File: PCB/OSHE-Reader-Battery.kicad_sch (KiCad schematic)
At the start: 12 parts, among them Q1 PNP, U1 BQ2057CSNTR, U2 IRF7326D2TRPBF

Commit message: Update OSHE-Reader-Battery.kicad_sch
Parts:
- R3: value R_{T2}/100K -> R_{T2}/10K
- R4: value R_{T1}/100K -> R_{T1}/10K
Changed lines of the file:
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@@
 			)
 		)
-		(property "Value" "R_{T1}/100K"
+		(property "Value" "R_{T1}/10K"
 			(at 41.91 107.9499 0)
 			(effects
@@
 			)
 		)
-		(property "Value" "R_{T2}/100K"
+		(property "Value" "R_{T2}/10K"
 			(at 41.91 92.7099 0)
 			(effects

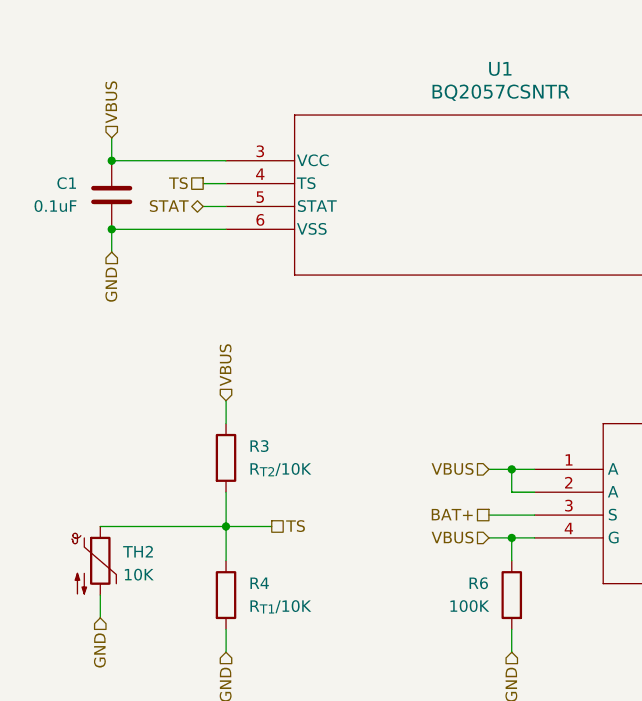
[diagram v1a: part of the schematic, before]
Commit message: removed old battery and thermistor references
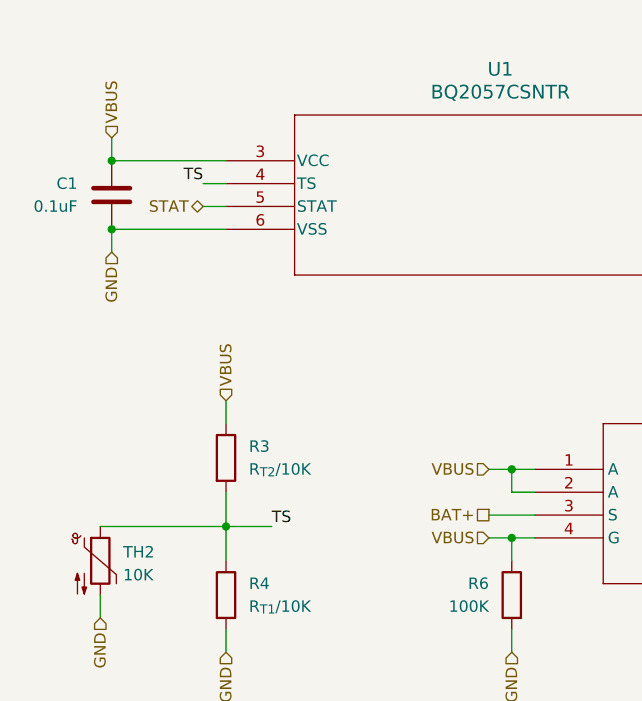
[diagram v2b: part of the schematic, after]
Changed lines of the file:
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@@
+		)
+	)
+	(label "TS"
+		(at 44.45 99.06 0)
+		(effects
+			(font
+				(size 1.27 1.27)
+			)
+			(justify left bottom)
+		)
+	)
+	(label "TS"
+		(at 36.83 60.96 180)
+		(effects
+			(font
+				(size 1.27 1.27)
+			)
+			(justify right bottom)
 		)
 	)
@@
 		)
 	)
-	(hierarchical_label "TS"
-		(shape passive)
-		(at 44.45 99.06 0)
-		(effects
-			(font
-				(size 1.27 1.27)
-			)
-			(justify left)
-		)
-	)
 	(hierarchical_label "VBUS"
 		(shape input)
@@
 		)
 	)
-	(hierarchical_label "TS"
-		(shape passive)
-		(at 36.83 60.96 180)
-		(effects
-			(font
-				(size 1.27 1.27)
-			)
-			(justify right)
-		)
-	)

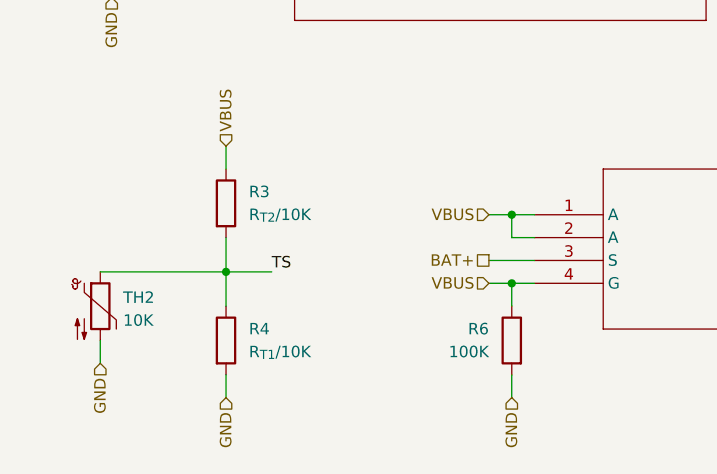
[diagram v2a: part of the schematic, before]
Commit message: Update OSHE-Reader-Battery.kicad_sch
changing resistor value for the thermstor
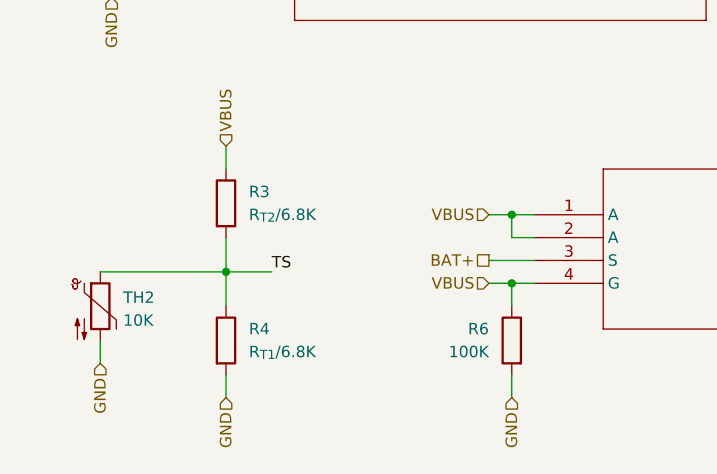
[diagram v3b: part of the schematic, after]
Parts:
- R3: value R_{T2}/10K -> R_{T2}/6.8K
- R4: value R_{T1}/10K -> R_{T1}/6.8K
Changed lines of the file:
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@@
 			)
 		)
-		(property "Value" "R_{T1}/10K"
+		(property "Value" "R_{T1}/6.8K"
 			(at 41.91 107.9499 0)
 			(effects
@@
 			)
 		)
-		(property "Value" "R_{T2}/10K"
+		(property "Value" "R_{T2}/6.8K"
 			(at 41.91 92.7099 0)
 			(effects

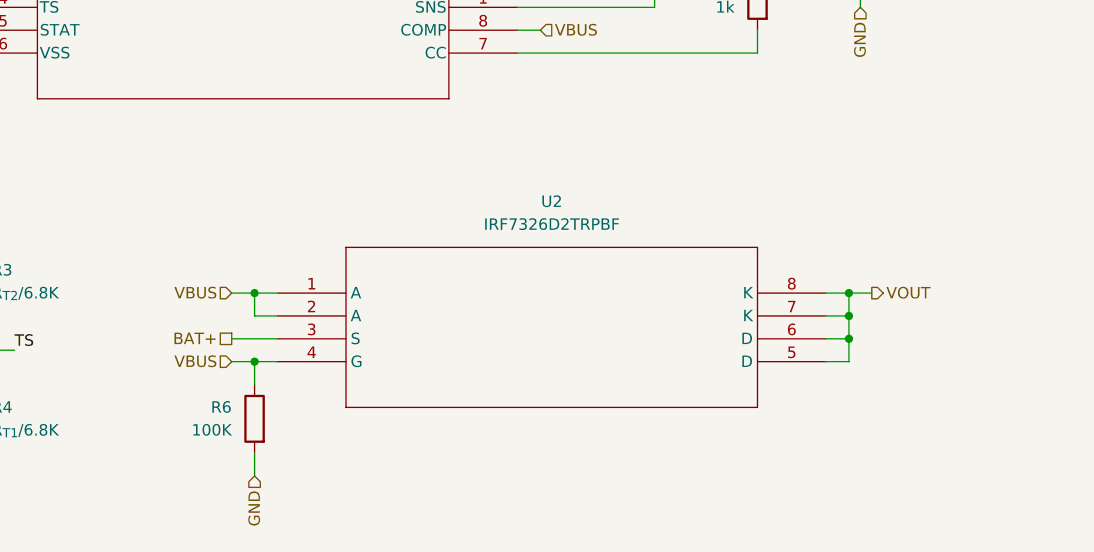
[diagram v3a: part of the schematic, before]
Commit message: Added LED to battery charger
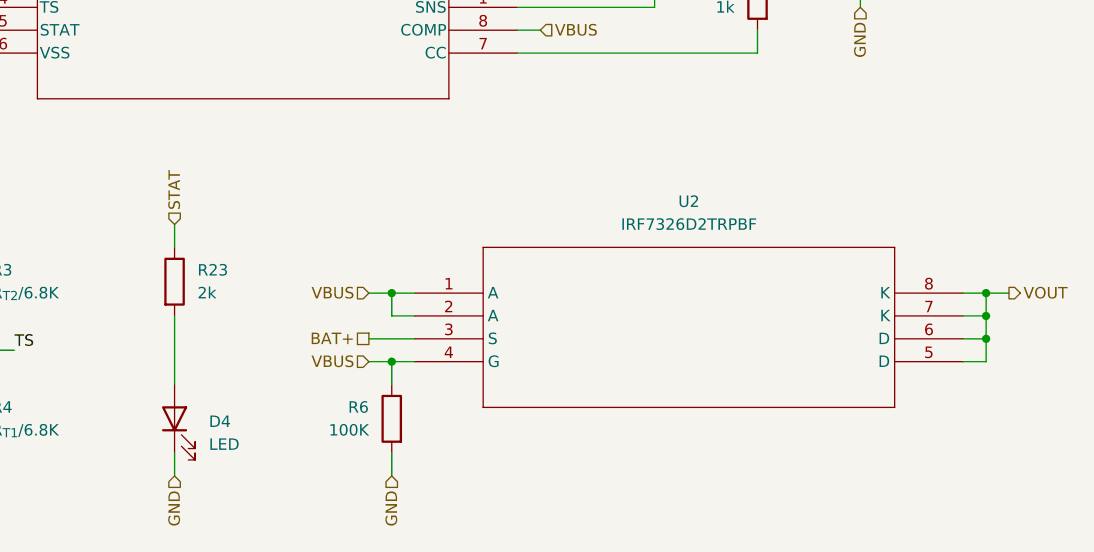
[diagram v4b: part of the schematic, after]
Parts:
- added D4: LED, symbol Device:LED
- added R23: 2k, symbol Device:R
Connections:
- net GND: now also D4.1 (K)
- net STAT: now also R23.1
- new net: D4.2 (A), R23.2
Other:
- moved on the sheet: R6, U2

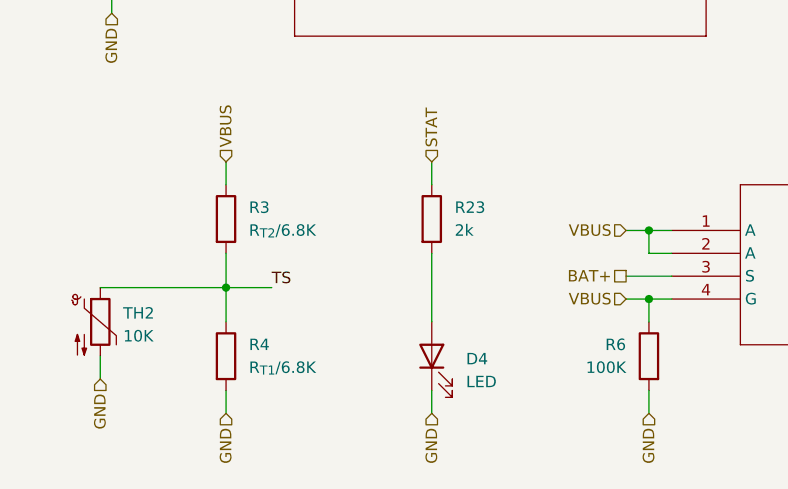
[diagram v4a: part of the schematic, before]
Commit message: Footprints added
All footprints added (problem with J1 for some reason) ((pads of the display driver))
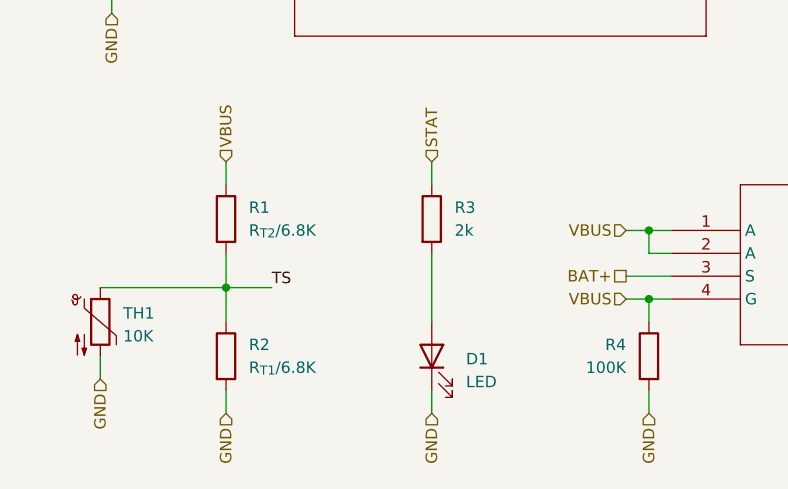
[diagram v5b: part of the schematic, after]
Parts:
- C1, C2: footprint (none) -> Capacitor_SMD:C_1206_3216Metric
- D1: renamed from D4; footprint (none) -> LED_SMD:LED_1206_3216Metric
- Q1: footprint (none) -> Package_TO_SOT_THT:TO-92_Inline
- R2: renamed from R4; footprint (none) -> Resistor_SMD:R_1206_3216Metric
- R3: renamed from R23; footprint (none) -> Resistor_SMD:R_1206_3216Metric
- R4: renamed from R6; footprint (none) -> Resistor_SMD:R_1206_3216Metric
- R5: footprint (none) -> Resistor_SMD:R_1206_3216Metric
- TH1: renamed from TH2; footprint (none) -> Resistor_THT:R_Axial_DIN0204_L3.6mm_D1.6mm_P5.08mm_Vertical
- renumbered R3 to R1
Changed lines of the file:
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@@
 		)
 		(instances
+			(project "OSHE-Reader-Battery"
+				(path "/0e6b7f01-01db-4a40-bfc7-232b1ad59e06"
+					(reference "U2")
+					(unit 1)
+				)
+			)
 			(project ""
 				(path "/3f072c92-e35a-4654-839b-728bd3dc3a46/9b683008-b3f5-4049-bcf9-7e8cdd298ddd"
@@
 			)
 		)
-		(property "Footprint" ""
+		(property "Footprint" "Resistor_SMD:R_1206_3216Metric"
 			(at 128.778 59.69 90)
 			(effects
@@
 		)
 		(instances
+			(project "OSHE-Reader-Battery"
+				(path "/0e6b7f01-01db-4a40-bfc7-232b1ad59e06"
+					(reference "R5")
+					(unit 1)
+				)
+			)
 			(project "OSHE-Reader-PCB"
 				(path "/3f072c92-e35a-4654-839b-728bd3dc3a46/9b683008-b3f5-4049-bcf9-7e8cdd298ddd"
@@
 		)
 		(instances
+			(project "OSHE-Reader-Battery"
+				(path "/0e6b7f01-01db-4a40-bfc7-232b1ad59e06"
+					(reference "R_{SNS}1")
+					(unit 1)
+				)
+			)
 			(project "OSHE-Reader-PCB"
 				(path "/3f072c92-e35a-4654-839b-728bd3dc3a46/9b683008-b3f5-4049-bcf9-7e8cdd298ddd"
@@
 		(dnp no)
 		(fields_autoplaced yes)
-		(property "Reference" "R4"
+		(property "Reference" "R2"
 			(at 41.91 105.4099 0)
 			(effects
@@
 			)
 		)
-		(property "Footprint" ""
+		(property "Footprint" "Resistor_SMD:R_1206_3216Metric"
 			(at 37.592 106.68 90)
 			(effects
@@
 		)
 		(instances
+			(project "OSHE-Reader-Battery"
+				(path "/0e6b7f01-01db-4a40-bfc7-232b1ad59e06"
+					(reference "R2")
+					(unit 1)
+				)
+			)
 			(project ""
 				(path "/3f072c92-e35a-4654-839b-728bd3dc3a46/9b683008-b3f5-4049-bcf9-7e8cdd298ddd"
@@
 		(dnp no)
 		(fields_autoplaced yes)
-		(property "Reference" "TH2"
+		(property "Reference" "TH1"
 			(at 27.94 101.9174 0)
 			(effects
@@
 			)
 		)
-		(property "Footprint" ""
+		(property "Footprint" "Resistor_THT:R_Axial_DIN0204_L3.6mm_D1.6mm_P5.08mm_Vertical"
 			(at 25.4 101.6 0)
 			(effects
@@
 		)
 		(instances
+			(project "OSHE-Reader-Battery"
+				(path "/0e6b7f01-01db-4a40-bfc7-232b1ad59e06"
+					(reference "TH1")
+					(unit 1)
+				)
+			)
 			(project ""
 				(path "/3f072c92-e35a-4654-839b-728bd3dc3a46/9b683008-b3f5-4049-bcf9-7e8cdd298ddd"
@@
 		(dnp no)
 		(fields_autoplaced yes)
-		(property "Reference" "D4"
+		(property "Reference" "D1"
 			(at 66.04 106.9974 90)
 			(effects
@@
 			)
 		)
-		(property "Footprint" ""
+		(property "Footprint" "LED_SMD:LED_1206_3216Metric"
 			(at 62.23 106.68 0)
 			(effects
@@
 		)
 		(instances
+			(project "OSHE-Reader-Battery"
+				(path "/0e6b7f01-01db-4a40-bfc7-232b1ad59e06"
+					(reference "D1")
+					(unit 1)
+				)
+			)
 			(project ""
 				(path "/3f072c92-e35a-4654-839b-728bd3dc3a46/9b683008-b3f5-4049-bcf9-7e8cdd298ddd"
@@
 		)
 		(instances
+			(project "OSHE-Reader-Battery"
+				(path "/0e6b7f01-01db-4a40-bfc7-232b1ad59e06"
+					(reference "U1")
+					(unit 1)
+				)
+			)
 			(project "OSHE-Reader-PCB"
 				(path "/3f072c92-e35a-4654-839b-728bd3dc3a46/9b683008-b3f5-4049-bcf9-7e8cdd298ddd"
@@
 		(on_board yes)
 		(dnp no)
-		(property "Reference" "R6"
+		(property "Reference" "R4"
 			(at 83.82 105.4099 0)
 			(effects
@@
 			)
 		)
-		(property "Footprint" ""
+		(property "Footprint" "Resistor_SMD:R_1206_3216Metric"
 			(at 88.138 106.68 90)
 			(effects
@@
 		)
 		(instances
+			(project "OSHE-Reader-Battery"
+				(path "/0e6b7f01-01db-4a40-bfc7-232b1ad59e06"
+					(reference "R4")
+					(unit 1)
+				)
+			)
 			(project "OSHE-Reader-PCB"
 				(path "/3f072c92-e35a-4654-839b-728bd3dc3a46/9b683008-b3f5-4049-bcf9-7e8cdd298ddd"
@@
 			)
 		)
-		(property "Footprint" ""
+		(property "Footprint" "Capacitor_SMD:C_1206_3216Metric"
 			(at 139.3952 55.88 0)
 			(effects
@@
 		)
 		(instances
+			(project "OSHE-Reader-Battery"
+				(path "/0e6b7f01-01db-4a40-bfc7-232b1ad59e06"
+					(reference "C2")
+					(unit 1)
+				)
+			)
 			(project "OSHE-Reader-PCB"
 				(path "/3f072c92-e35a-4654-839b-728bd3dc3a46/9b683008-b3f5-4049-bcf9-7e8cdd298ddd"
@@
 			)
 		)
-		(property "Footprint" ""
+		(property "Footprint" "Package_TO_SOT_THT:TO-92_Inline"
 			(at 127 12.7 0)
 			(effects
@@
 		)
 		(instances
+			(project "OSHE-Reader-Battery"
+				(path "/0e6b7f01-01db-4a40-bfc7-232b1ad59e06"
+					(reference "Q1")
+					(unit 1)
+				)
+			)
 			(project "OSHE-Reader-PCB"
 				(path "/3f072c92-e35a-4654-839b-728bd3dc3a46/9b683008-b3f5-4049-bcf9-7e8cdd298ddd"
@@
 		(dnp no)
 		(fields_autoplaced yes)
-		(property "Reference" "R3"
+		(property "Reference" "R1"
 			(at 41.91 90.1699 0)
 			(effects
@@
 		)
 		(instances
+			(project "OSHE-Reader-Battery"
+				(path "/0e6b7f01-01db-4a40-bfc7-232b1ad59e06"
+					(reference "R1")
+					(unit 1)
+				)
+			)
 			(project "OSHE-Reader-PCB"
 				(path "/3f072c92-e35a-4654-839b-728bd3dc3a46/9b683008-b3f5-4049-bcf9-7e8cdd298ddd"
@@
 			)
 		)
-		(property "Footprint" ""
+		(property "Footprint" "Capacitor_SMD:C_1206_3216Metric"
 			(at 25.7048 66.04 0)
 			(effects
@@
 		)
 		(instances
+			(project "OSHE-Reader-Battery"
+				(path "/0e6b7f01-01db-4a40-bfc7-232b1ad59e06"
+					(reference "C1")
+					(unit 1)
+				)
+			)
 			(project "OSHE-Reader-PCB"
 				(path "/3f072c92-e35a-4654-839b-728bd3dc3a46/9b683008-b3f5-4049-bcf9-7e8cdd298ddd"
@@
 		(dnp no)
 		(fields_autoplaced yes)
-		(property "Reference" "R23"
+		(property "Reference" "R3"
 			(at 64.77 90.1699 0)
 			(effects
@@
 			)
 		)
-		(property "Footprint" ""
+		(property "Footprint" "Resistor_SMD:R_1206_3216Metric"
 			(at 60.452 91.44 90)
 			(effects
@@
 		)
 		(instances
+			(project "OSHE-Reader-Battery"
+				(path "/0e6b7f01-01db-4a40-bfc7-232b1ad59e06"
+					(reference "R3")
+					(unit 1)
+				)
+			)
 			(project ""
 				(path "/3f072c92-e35a-4654-839b-728bd3dc3a46/9b683008-b3f5-4049-bcf9-7e8cdd298ddd"
@@
 		)
 		(instances
+			(project "OSHE-Reader-Battery"
+				(path "/0e6b7f01-01db-4a40-bfc7-232b1ad59e06"
+					(reference "R_{SNS}2")
+					(unit 1)
+				)
+			)
 			(project "OSHE-Reader-PCB"
 				(path "/3f072c92-e35a-4654-839b-728bd3dc3a46/9b683008-b3f5-4049-bcf9-7e8cdd298ddd"
@@
 		)
 	)
+	(sheet_instances
+		(path "/"
+			(page "1")
+		)
+	)
+	(embedded_fonts no)
 )

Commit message: Did a bunch of work with final preparations of the schematic for pcb routing
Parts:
- removed D1: LED, LED_SMD:LED_1206_3216Metric, symbol Device:LED
- added J4: S2B-PH-K-SLFSN, S2B_PH_K_S_LF__SN_:CONN_S2B-PH-K-S_JST, symbol S2B_PH_K_S_LF__SN_:S2B-PH-K-SLFSN
- added LED1: HSMY-C110, LED3_HSMx-C110_AVA, symbol ul_HSMY-C110:HSMY-C110
- R3: renamed from R1; footprint (none) -> Resistor_SMD:R_1206_3216Metric
- renumbered R3 to R23, R2 to R4, R4 to R6, TH1 to TH2
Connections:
- net BAT+: now also J4.1
- net GND: now also J4.2, LED1.1
- net at R23.2: now also LED1.3
- no-connect marks 0 -> 1
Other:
- moved on the sheet: R23, R6, U2

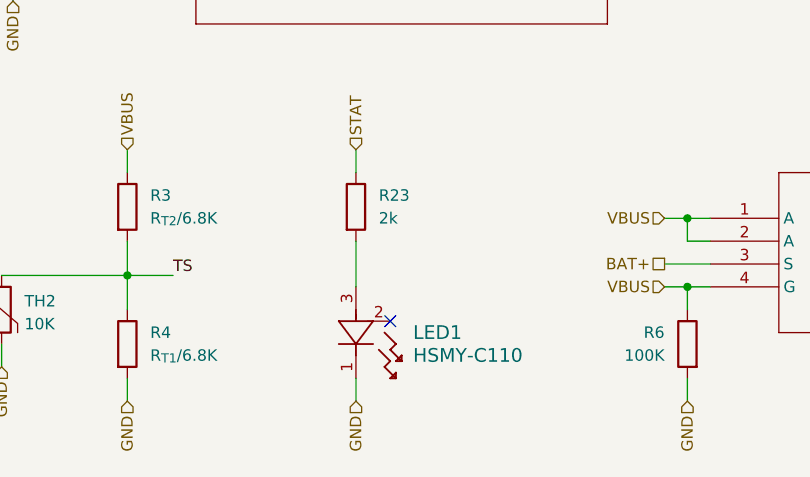
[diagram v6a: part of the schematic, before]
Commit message: Started routing PCB & added case dxf for reference
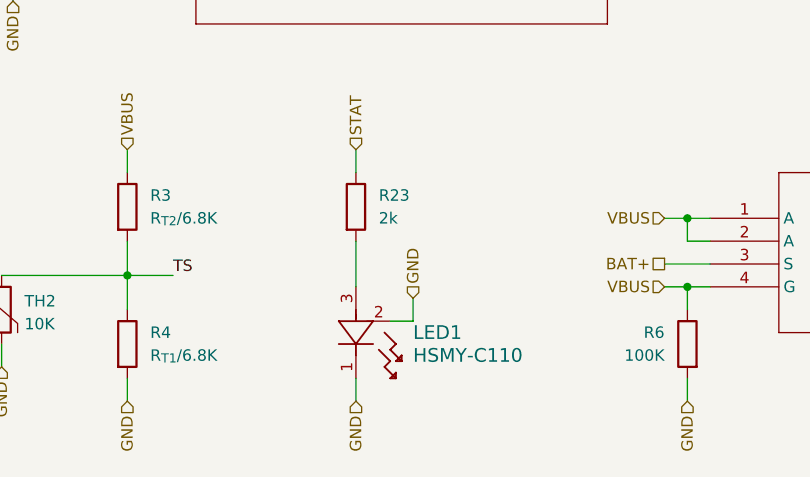
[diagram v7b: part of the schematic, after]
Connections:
- net GND: now also LED1.2
- no-connect marks 1 -> 0
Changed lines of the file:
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@@
 		(color 0 0 0 0)
 	)
-	(no_connect
-		(at 68.58 104.14)
-	)
 	(wire
 		(pts
@@
 	(wire
 		(pts
+			(xy 71.12 104.14) (xy 71.12 101.6)
+		)
+		(stroke
+			(width 0)
+			(type default)
+		)
+	)
+	(wire
+		(pts
 			(xy 64.77 85.09) (xy 64.77 87.63)
 		)
@@
 		(pts
 			(xy 115.57 45.72) (xy 113.03 45.72)
+		)
+		(stroke
+			(width 0)
+			(type default)
+		)
+	)
+	(wire
+		(pts
+			(xy 68.58 104.14) (xy 71.12 104.14)
 		)
 		(stroke
@@
 		)
 	)
+	(hierarchical_label "GND"
+		(shape input)
+		(at 71.12 101.6 90)
+		(effects
+			(font
+				(size 1.27 1.27)
+			)
+			(justify left)
+		)
+	)
